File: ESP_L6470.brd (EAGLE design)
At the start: 41.9 x 90.2 mm, 41 parts, among them IC2 CP2104, J1 MICRO-USB, J2 POWER_JACKPTH_LOCK, Q1 600mA/40V, Q2 600mA/40V, U1 L6470, U2 ESP-WROOM-03, U3 RGB-LED

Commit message: Updated board
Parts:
- added U$13: INTERFACE_NETSTEPPER, IAD_GRAPHIC:INTERFACE_NETSTEPPER
- added U$15: ZHDK_LOGO_METAL, IAD_GRAPHIC:ZHDK_LOGO
- moved J2 1.02 mm to (47.0, 36.2)
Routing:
- net VS: track 137.2 -> 136.2 mm
- net GND: track 106.0 -> 105.1 mm
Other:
- board text removed: "1A"
- board text removed: "1B"
- board text removed: "2018"
- board text removed: "2A"
- board text removed: "2B"
- board text removed: "8-36V"
- board text removed: "DOWN"
- board text removed: "ENCODER"
- board text removed: "HOME"
- board text removed: "JOEL GÄHWILER"
- board text removed: "LUKE FRANZKE"
- board text removed: "STOP"
- board text removed: "STOP1"
- board text removed: "STOP2"
- board text removed: "UP"
- board text removed: "ZHDK IAD"
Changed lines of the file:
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@@
 <board>
 <plain>
-<text x="31.369" y="85.09" size="1.016" layer="21" font="vector" ratio="15" rot="R180">1B</text>
-<text x="26.289" y="85.09" size="1.016" layer="21" font="vector" ratio="15" rot="R180">1A</text>
-<text x="33.909" y="85.09" size="1.016" layer="21" font="vector" ratio="15" rot="R180">2B</text>
-<text x="28.829" y="85.09" size="1.016" layer="21" font="vector" ratio="15" rot="R180">2A</text>
 <polygon width="0.2032" layer="30">
 <vertex x="22.86" y="62.23"/>
@@
 <vertex x="35.56" y="62.23"/>
 </polygon>
-<text x="35.814" y="29.21" size="1.27" layer="21" font="vector" ratio="15" align="bottom-center">8-36V</text>
-<wire x1="28.829" y1="89.662" x2="28.829" y2="90.932" width="0.254" layer="21"/>
-<wire x1="23.749" y1="89.662" x2="23.749" y2="90.932" width="0.254" layer="21"/>
-<wire x1="23.749" y1="90.932" x2="25.019" y2="90.932" width="0.254" layer="21" curve="-180"/>
-<wire x1="25.019" y1="90.932" x2="26.289" y2="90.932" width="0.254" layer="21" curve="-180"/>
-<wire x1="26.289" y1="90.932" x2="27.559" y2="90.932" width="0.254" layer="21" curve="-180"/>
-<wire x1="27.559" y1="90.932" x2="28.829" y2="90.932" width="0.254" layer="21" curve="-180"/>
-<wire x1="34.544" y1="89.662" x2="34.544" y2="90.932" width="0.254" layer="21"/>
-<wire x1="29.464" y1="89.662" x2="29.464" y2="90.932" width="0.254" layer="21"/>
-<wire x1="29.464" y1="90.932" x2="30.734" y2="90.932" width="0.254" layer="21" curve="-180"/>
-<wire x1="30.734" y1="90.932" x2="32.004" y2="90.932" width="0.254" layer="21" curve="-180"/>
 <wire x1="32.004" y1="90.932" x2="33.274" y2="90.932" width="0.254" layer="21" curve="-180"/>
-<wire x1="33.274" y1="90.932" x2="34.544" y2="90.932" width="0.254" layer="21" curve="-180"/>
-<text x="12.827" y="15.875" size="1.778" layer="21" rot="R180" align="bottom-center">UP</text>
-<text x="31.877" y="6.096" size="1.778" layer="21" rot="R180" align="bottom-center">STOP</text>
-<text x="12.827" y="6.096" size="1.778" layer="21" rot="R180" align="bottom-center">DOWN</text>
-<text x="22.098" y="6.096" size="1.778" layer="21" rot="R180" align="bottom-center">HOME</text>
 <wire x1="43.18" y1="5.08" x2="43.18" y2="90.17" width="0.1524" layer="20"/>
 <wire x1="43.18" y1="90.17" x2="40.64" y2="92.71" width="0.1524" layer="20" curve="90"/>
@@
 <wire x1="3.81" y1="2.54" x2="40.64" y2="2.54" width="0.1524" layer="20"/>
 <wire x1="40.64" y1="2.54" x2="43.18" y2="5.08" width="0.1524" layer="20" curve="90"/>
-<text x="35.56" y="14.224" size="1.27" layer="21" font="vector" ratio="15" rot="R90" align="top-left">ZHDK IAD</text>
-<text x="37.338" y="14.224" size="1.27" layer="21" font="vector" ratio="15" rot="R90" align="top-left">LUKE FRANZKE</text>
-<text x="39.116" y="14.224" size="1.27" layer="21" font="vector" ratio="15" rot="R90" align="top-left">JOEL GÄHWILER  </text>
-<text x="40.64" y="14.224" size="1.27" layer="21" font="vector" ratio="15" rot="R90" align="top-left">2018</text>
-<text x="3.302" y="18.669" size="1.27" layer="21" font="vector" ratio="15" rot="R90" align="top-left">ENCODER</text>
-<text x="3.302" y="33.909" size="1.27" layer="21" font="vector" ratio="15" rot="R90" align="top-left">STOP1</text>
-<text x="3.302" y="44.069" size="1.27" layer="21" font="vector" ratio="15" rot="R90" align="top-left">STOP2</text>
 </plain>
 <attributes>
@@
 <attribute name="PROD_ID" value="CONN-09696" x="25.4" y="87.63" size="1.778" layer="27" display="off"/>
 </element>
-<element name="J2" library="SparkFun-Connectors" package="POWER_JACK_PTH_LOCK" value="POWER_JACKPTH_LOCK" x="46.99" y="35.179" rot="R90">
-<attribute name="PROD_ID" value="CONN-08197" x="46.99" y="35.179" size="1.778" layer="27" rot="R90" display="off"/>
-<attribute name="SF_ID" value="PRT-00119" x="46.99" y="35.179" size="1.778" layer="27" rot="R90" display="off"/>
+<element name="J2" library="SparkFun-Connectors" package="POWER_JACK_PTH_LOCK" value="POWER_JACKPTH_LOCK" x="46.99" y="36.195" rot="R90">
+<attribute name="PROD_ID" value="CONN-08197" x="46.99" y="36.195" size="1.778" layer="27" rot="R90" display="off"/>
+<attribute name="SF_ID" value="PRT-00119" x="46.99" y="36.195" size="1.778" layer="27" rot="R90" display="off"/>
 </element>
 <element name="U$18" library="IAD-Library" package="B3AL-1002P-MS" value="B3AL-1002P-MS" x="12.7" y="10.16" rot="R180"/>
@@
 <element name="U$11" library="RP400N501A" package="STAND-OFF" value="" x="40.64" y="90.17"/>
 <element name="U$12" library="RP400N501A" package="STAND-OFF" value="" x="3.81" y="90.17"/>
+<element name="U$13" library="IAD_GRAPHIC" package="INTERFACE_NETSTEPPER" value="INTERFACE_NETSTEPPER" x="3.81" y="5.08"/>
+<element name="U$15" library="IAD_GRAPHIC" package="ZHDK_LOGO" value="ZHDK_LOGO_METAL" x="8.89" y="81.28" rot="R90"/>
 </elements>
 <signals>
@@
 <contactref element="J2" pad="GND"/>
 <contactref element="J2" pad="GNDBREAK"/>
-<wire x1="36.29" y1="38.9406" x2="40.0262" y2="36.4744" width="1.016" layer="1"/>
-<wire x1="40.0262" y1="36.4744" x2="40.433" y2="35.2044" width="1.016" layer="1"/>
-<wire x1="36.29" y1="38.9406" x2="38.8784" y2="41.91" width="1.016" layer="1"/>
+<wire x1="36.29" y1="39.9566" x2="40.0262" y2="36.4744" width="1.016" layer="1"/>
+<wire x1="40.0262" y1="36.4744" x2="40.433" y2="36.2204" width="1.016" layer="1"/>
+<wire x1="36.29" y1="39.9566" x2="38.8784" y2="41.91" width="1.016" layer="1"/>
 <wire x1="38.8784" y1="41.91" x2="38.8784" y2="51.9816" width="1.016" layer="1"/>
 <wire x1="38.8784" y1="51.9816" x2="36.83" y2="54.03" width="1.016" layer="1"/>
@@
 <wire x1="40.64" y1="74.93" x2="41.91" y2="73.66" width="0.8128" layer="16"/>
 <contactref element="J2" pad="PWR"/>
-<wire x1="33.1122" y1="35.179" x2="33.1122" y2="41.8752" width="1.016" layer="1"/>
+<wire x1="33.1122" y1="36.195" x2="33.1122" y2="41.8752" width="1.016" layer="1"/>
 <wire x1="33.1122" y1="41.8752" x2="36.83" y2="45.72" width="1.016" layer="1"/>
 <wire x1="41.91" y1="59.69" x2="41.91" y2="50.8" width="1.016" layer="16"/>

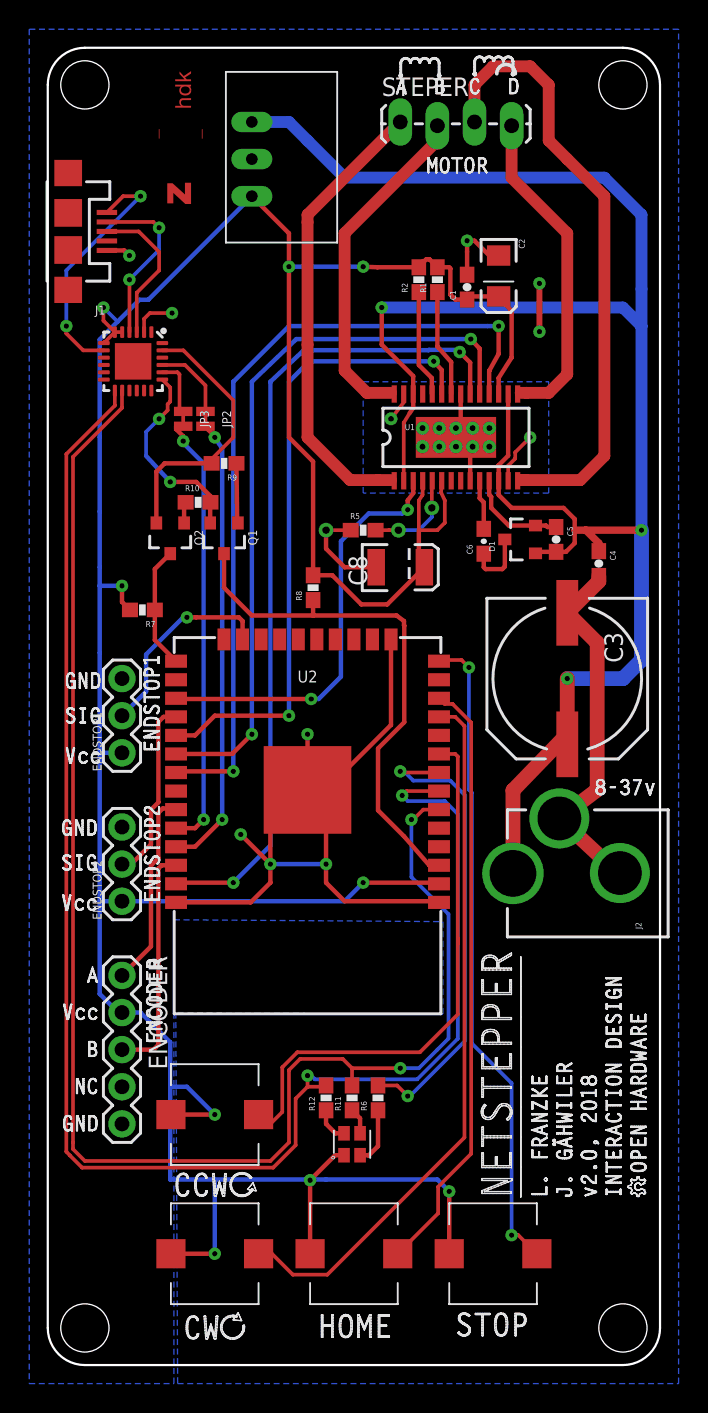
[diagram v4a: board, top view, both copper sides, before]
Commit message: Updated with silkscreen
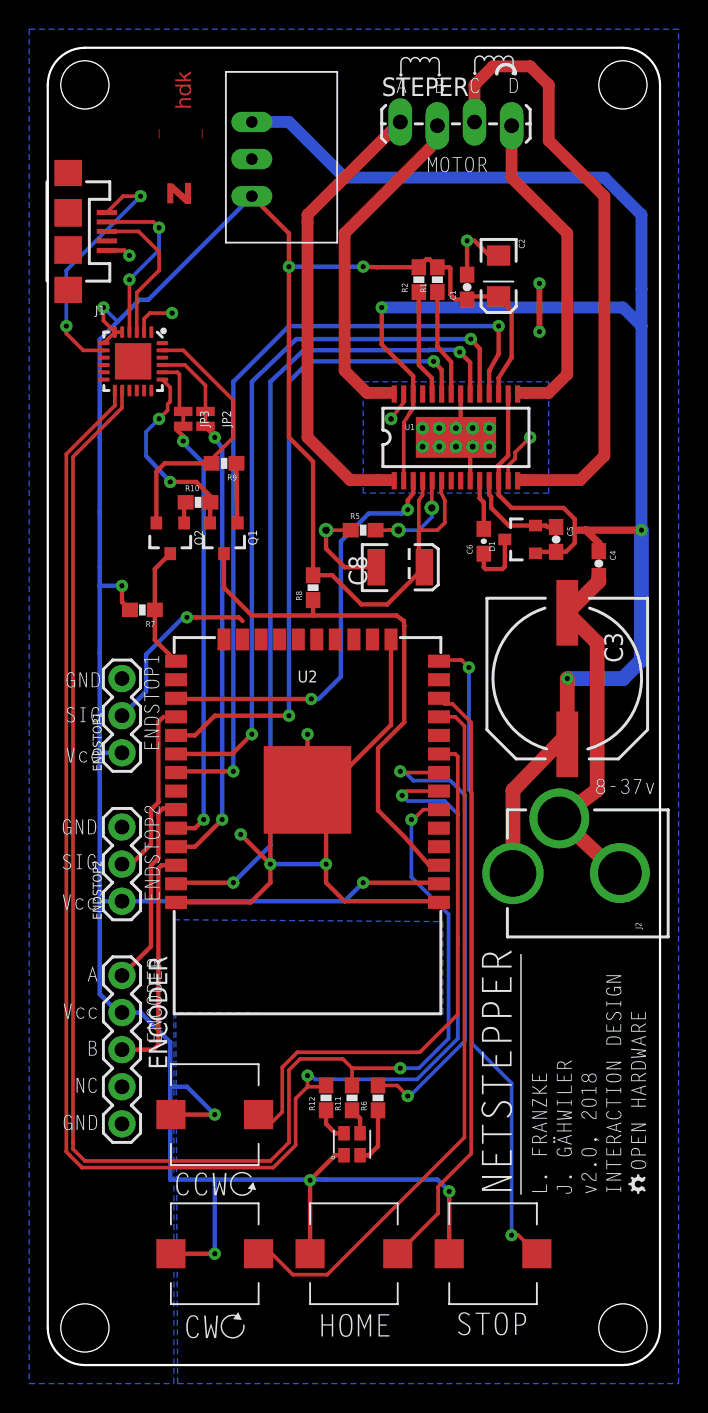
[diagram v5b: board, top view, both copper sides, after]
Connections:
- new net ESTOP1: U2.23
- new net ESTOP2: U2.28
- net ENDSTOP1: no longer U2.23
- net ENDSTOP2: no longer U2.28
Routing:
- net ENDSTOP1: track 13.9 -> 12.6 mm
- net ENDSTOP2: track 12.6 -> 11.7 mm
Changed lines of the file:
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@@
 <layer number="18" name="Vias" color="2" fill="1" visible="yes" active="yes"/>
 <layer number="19" name="Unrouted" color="6" fill="1" visible="yes" active="yes"/>
-<layer number="20" name="Dimension" color="15" fill="1" visible="yes" active="yes"/>
+<layer number="20" name="Dimension" color="15" fill="1" visible="no" active="yes"/>
 <layer number="21" name="tPlace" color="16" fill="1" visible="yes" active="yes"/>
 <layer number="22" name="bPlace" color="14" fill="1" visible="yes" active="yes"/>
@@
 <signal name="ENDSTOP1">
 <contactref element="ENDSTOP1" pad="2"/>
-<contactref element="U2" pad="23"/>
 <wire x1="14.605" y1="53.467" x2="14.351" y2="53.721" width="0.3048" layer="1"/>
 <wire x1="14.351" y1="53.721" x2="11.43" y2="53.721" width="0.3048" layer="1"/>
 <wire x1="11.43" y1="53.721" x2="10.795" y2="53.721" width="0.3048" layer="1"/>
-<wire x1="14.605" y1="52.21" x2="14.605" y2="53.467" width="0.3048" layer="1"/>
 <wire x1="8.001" y1="48.641" x2="8.001" y2="51.181" width="0.3048" layer="16"/>
 <wire x1="10.541" y1="53.721" x2="10.795" y2="53.721" width="0.3048" layer="16"/>
@@
 <contactref element="ENDSTOP2" pad="2"/>
 <wire x1="6.43" y1="36.75" x2="6.35" y2="36.83" width="0.3048" layer="1"/>
-<contactref element="U2" pad="28"/>
 <wire x1="6.35" y1="36.83" x2="6.985" y2="36.83" width="0.3048" layer="1"/>
 <wire x1="8.3348" y1="38.1798" x2="8.3348" y2="40.549225" width="0.3048" layer="1"/>
 <wire x1="8.3348" y1="40.549225" x2="8.8428" y2="41.057225" width="0.3048" layer="1"/>
 <wire x1="6.985" y1="36.83" x2="8.3348" y2="38.1798" width="0.3048" layer="1"/>
-<wire x1="9.191" y1="46.91" x2="10.05" y2="46.91" width="0.3048" layer="1"/>
 <wire x1="8.8428" y1="41.057225" x2="8.8428" y2="46.5618" width="0.3048" layer="1"/>
 <wire x1="8.8428" y1="46.5618" x2="9.191" y2="46.91" width="0.3048" layer="1"/>
@@
 <contactref element="U2" pad="32"/>
 </signal>
+<signal name="ESTOP1">
+<contactref element="U2" pad="23"/>
+</signal>
+<signal name="ESTOP2">
+<contactref element="U2" pad="28"/>
+</signal>
 </signals>
